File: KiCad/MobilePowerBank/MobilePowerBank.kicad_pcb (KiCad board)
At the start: 2 copper layers, 138 x 195 mm, 221 parts, among them J1 Power IN, J10 Power OUT 6, J2 Power OUT 2, J3 Power OUT 1, J4 OLED I2C, J5 PDI, J6 OLED, J7 Power OUT 3, J8 Power OUT 4, J9 Power OUT 5, SW1 SW_DIP_x01, U1 INA139, U10 INA139, U11 LMZ14201H, U12 LMZ14201H, U13 INA139, U14 INA139, U15 ATXMEGA256A3U-AU, U16 INA139, U2 LMZ14203H, U3 L78M12, U4 INA139, U5 UA78M33, U6 LMZ14203H, U7 LMZ14203H, U8 LMZ14203H, U9 INA139, x1 jumper, x2 jumper, x3 jumper, x4 jumper, x5 jumper, x6 jumper, x7 jumper, x8 jumper, x9 jumper

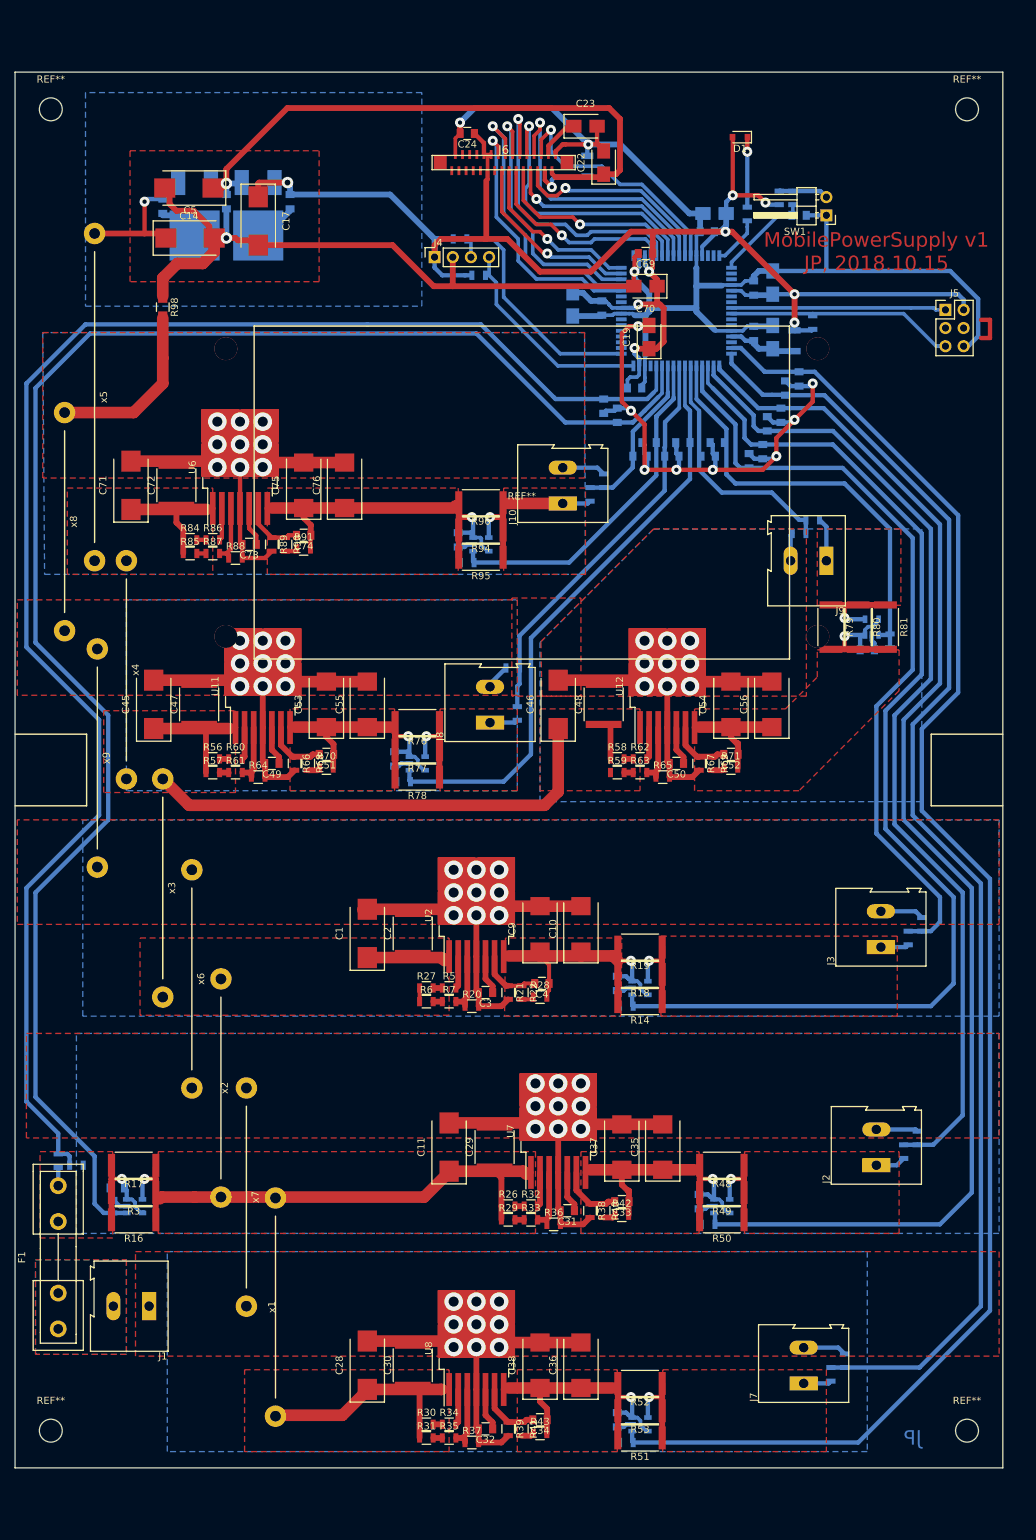
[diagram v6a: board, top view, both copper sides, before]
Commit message: Aligning PCB
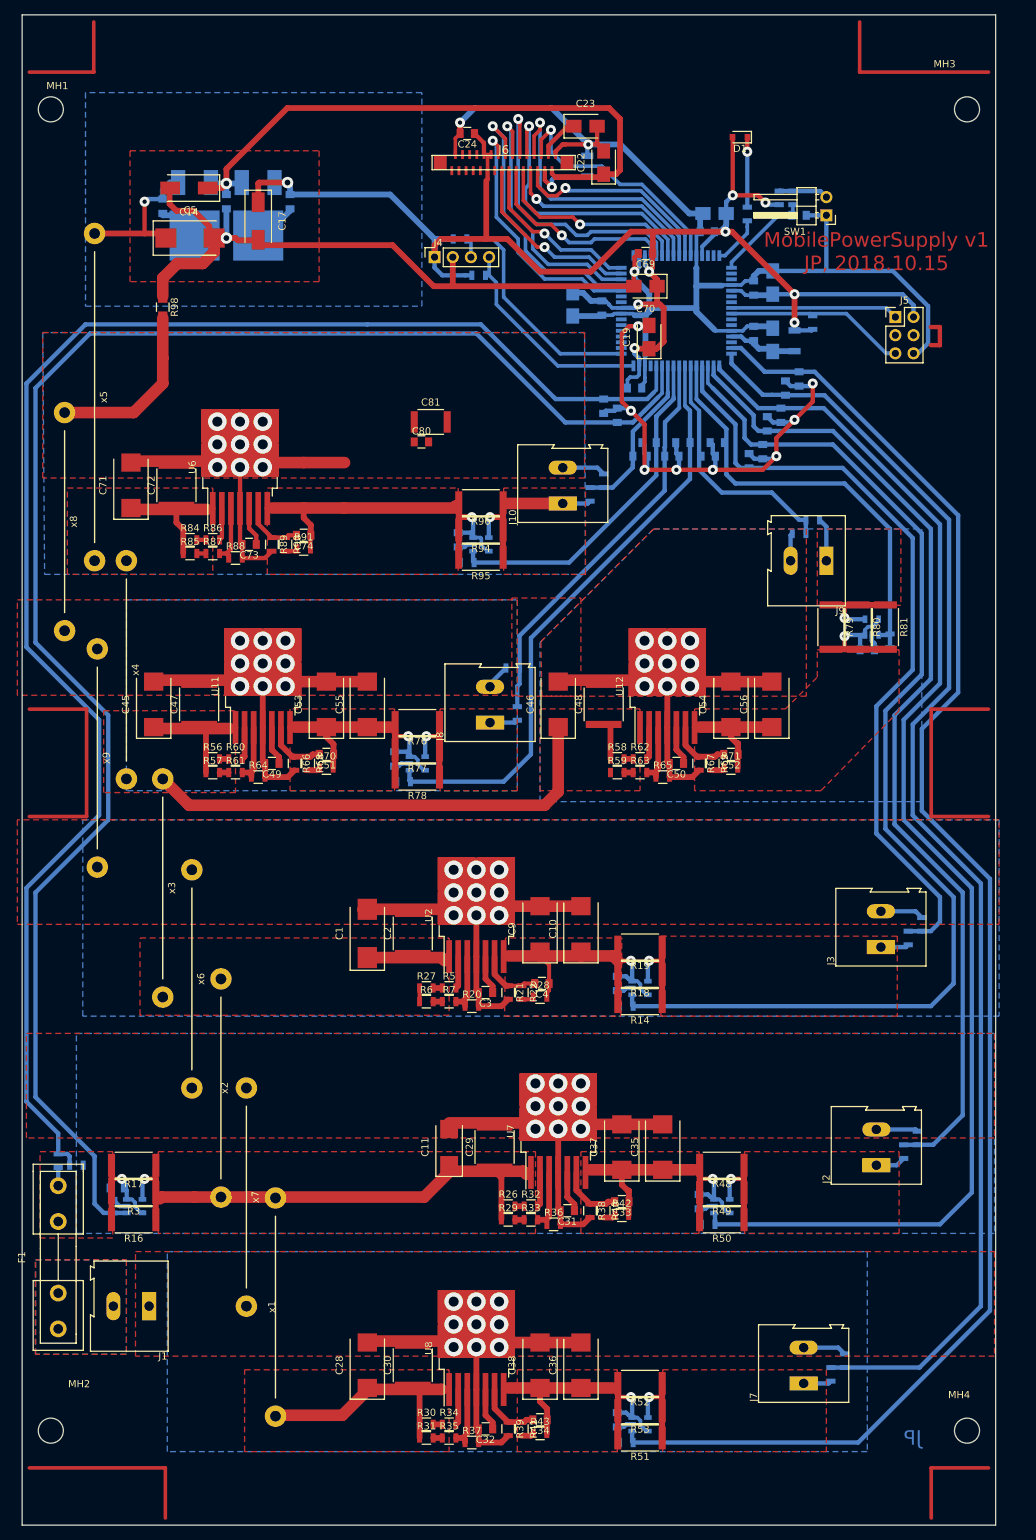
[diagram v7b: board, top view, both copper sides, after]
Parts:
- removed C75, C76: 47u/1-45mESR, Capacitors_Tantalum_SMD:CP_Tantalum_Case-D_EIA-7343-31_Reflow
- removed REF** (x4): MountingHole_3.2mm_M3, Mounting_Holes:MountingHole_3.2mm_M3
- removed REF**: RET012864LYPP3N, JPDisplays:RET012864LYPP3N
- added C80: 1u/50V, Capacitors_SMD:C_0805, F.Cu at (76.8, 71.7)
- added C81: 100u/6V3, Capacitors_SMD:C_1812, F.Cu at (78.1, 68.9)
- added MH1: MountingHole_Pad, Mounting_Holes:MountingHole_3.5mm, F.Cu at (25.9, 26.4)
- added MH2: MountingHole_Pad, Mounting_Holes:MountingHole_3.5mm, F.Cu at (29.0, 207.8)
- added MH3: MountingHole_Pad, Mounting_Holes:MountingHole_3.5mm, F.Cu at (149.9, 23.4)
- added MH4: MountingHole_Pad, Mounting_Holes:MountingHole_3.5mm, F.Cu at (151.9, 209.3)
- C11: footprint Capacitors_Tantalum_SMD:CP_Tantalum_Case-V_EIA-7343-20_Wave -> Capacitors_Tantalum_SMD:CP_Tantalum_Case-C_EIA-6032-28_Reflow
- C14, C17: footprint Capacitors_Tantalum_SMD:CP_Tantalum_Case-V_EIA-7343-20_Wave -> Capacitors_Tantalum_SMD:CP_Tantalum_Case-C_EIA-6032-28_Wave
- C2, C29, C30, C47, C48, C72: value 10u/35V/X7R -> 10u/50V/X7R
- C28, C45, C46, C71: footprint Capacitors_Tantalum_SMD:CP_Tantalum_Case-V_EIA-7343-20_Wave -> Capacitors_Tantalum_SMD:CP_Tantalum_Case-D_EIA-7343-31_Reflow
- C3: value 4u7 -> 4n7
- C31, C32: value 4u7 -> 10n
- C73: value 4u7 -> 22n
- R84: value 220k -> 0
- R85: value 47k -> 0
- R86: value 30k -> 100k
- R87: value 300k -> 68k
- R88: value 20k -> 11k
- R89: value 2k2 -> 1k5
- R90: value 15k4 -> 7k68
- R91: value 15k4 -> 200
- U6: value LMZ14203H -> LMZ14203
- moved J5 7.07 mm to (143.0, 54.2)
- moved C21 0.38 mm to (125.9, 57.4)
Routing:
- net (no net): track 5.08 -> 149.1 mm
- net PDI_DATA: track 30.0 -> 23.4 mm
- net GND: track 391.0 -> 384.5 mm
- net +3V3: track 236.7 -> 230.3 mm
- net PDI_CLK: track 33.1 -> 26.7 mm
- net /OLED_!DS: track 36.6 -> 35.9 mm
- net /OLED_D/!C: track 39.9 -> 39.3 mm
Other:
- board size 138 x 195 mm -> 136 x 211 mm

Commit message: Pimping PCB
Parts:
- C1, C5: footprint Capacitors_Tantalum_SMD:CP_Tantalum_Case-V_EIA-7343-20_Wave -> Capacitors_Tantalum_SMD:CP_Tantalum_Case-D_EIA-7343-31_Reflow
- C11: footprint Capacitors_Tantalum_SMD:CP_Tantalum_Case-C_EIA-6032-28_Reflow -> Capacitors_Tantalum_SMD:CP_Tantalum_Case-D_EIA-7343-31_Reflow
- C14, C17: footprint Capacitors_Tantalum_SMD:CP_Tantalum_Case-C_EIA-6032-28_Wave -> Capacitors_Tantalum_SMD:CP_Tantalum_Case-C_EIA-6032-28_Reflow
- C19, C21, C22, C23, C64, C66, C68, C70: footprint Capacitors_Tantalum_SMD:CP_Tantalum_Case-B_EIA-3528-21_Wave -> Capacitors_Tantalum_SMD:CP_Tantalum_Case-B_EIA-3528-21_Reflow
- C80: footprint Capacitors_SMD:C_0805 -> Capacitors_SMD:C_1206
- x1, x2, x3, x4, x6, x7, x8: footprint JPJumpers:Jumper_30x1.5 -> JPJumpers:Jumper_33x1.5
- x9: footprint JPJumpers:Jumper_30x1.5 -> JPJumpers:Jumper_45x1.5
- moved C80 17.7 mm to (59.1, 71.8), turned to 90 degrees
- moved C81 16.2 mm to (62.2, 72.4), turned to 90 degrees
- moved C39 13.5 mm to (134.0, 59.0)
- moved C43 13.5 mm to (135.9, 57.8)
- moved C27 13.1 mm to (132.7, 62.9)
- moved C26 13.1 mm to (130.8, 64.1)
- moved J4 12.4 mm to (85.7, 35.7)
- moved C20 12.3 mm to (130.2, 46.4)
- moved C21 12.3 mm to (132.8, 47.2)
- moved C44 12.3 mm to (136.5, 52.7)
- moved J5 12.3 mm to (150.0, 44.1)
- moved C23 12.3 mm to (106.7, 17.4)
- moved C65 12.3 mm to (130.2, 40.0)
- moved C66 12.3 mm to (132.8, 39.2)
- moved R24 12.3 mm to (138.4, 44.8)
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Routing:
- net GNDA: track 424.9 -> 463.8 mm
- net IN_Current: track 232.2 -> 253.7 mm
- net IN_Voltage: track 220.5 -> 241.0 mm
- net OUT_3_Current: track 217.7 -> 237.0 mm
- net OUT_3_Voltage: track 181.2 -> 196.1 mm
- net OUT_2_Current: track 179.0 -> 193.3 mm
- net OUT_2_Voltage: track 139.4 -> 152.6 mm
- net +3V3: track 230.3 -> 219.0 mm, vias 9 -> 7
- net OUT_6_Voltage: track 23.4 -> 33.8 mm
- net GND: track 384.5 -> 374.6 mm
- net OUT_6_Current: track 48.5 -> 57.8 mm
- net OUT_4_Current: track 83.8 -> 93.2 mm
- net OUT_1_Current: track 159.1 -> 168.1 mm
- net OUT_1_Voltage: track 109.0 -> 117.7 mm
- net OUT_4_Voltage: track 57.0 -> 65.5 mm
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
